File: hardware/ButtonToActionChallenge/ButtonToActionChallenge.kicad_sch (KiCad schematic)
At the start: 4 parts, among them J1 ActionOutput, J2 Button Wires, J3 ActionOutput, J4 ActionTrigger

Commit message: updating button to action challenge PCB to use 12v for button LED
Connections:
- net +12V: now also J2.3 (Pin_3)
- net +5V: no longer J2.3 (Pin_3)

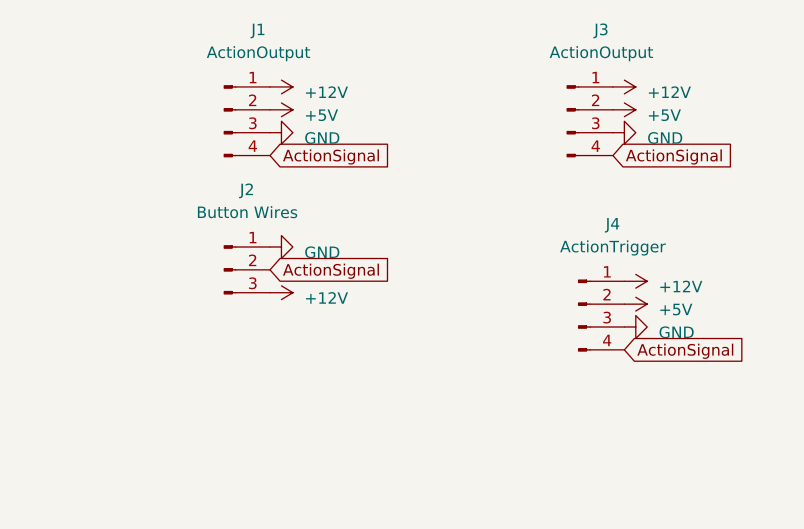
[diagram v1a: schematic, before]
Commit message: Updated Action Challenge Connector Board
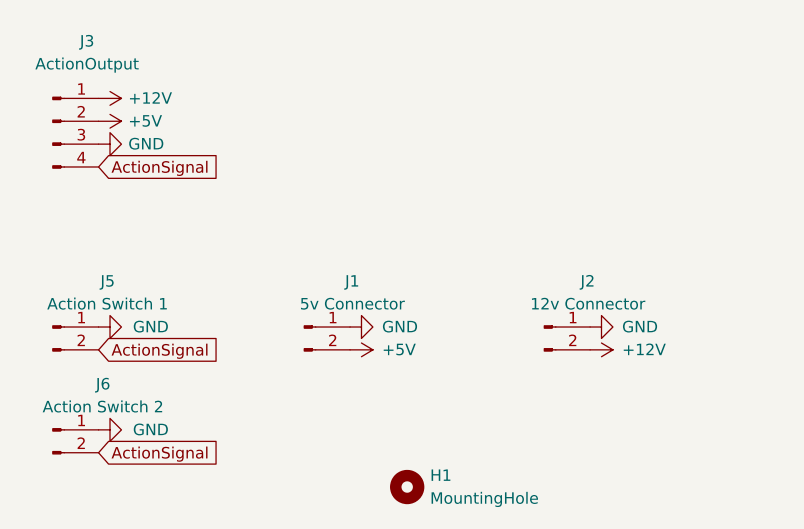
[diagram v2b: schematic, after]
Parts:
- removed J1: ActionOutput, Connector_JST:JST_PH_B4B-PH-K_1x04_P2.00mm_Vertical, symbol Connector:Conn_01x04_Pin
- removed J2: Button Wires, Connector_JST:JST_XH_B3B-XH-A_1x03_P2.50mm_Vertical, symbol Connector:Conn_01x03_Pin
- removed J4: ActionTrigger, Connector_JST:JST_PH_B4B-PH-K_1x04_P2.00mm_Vertical, symbol Connector:Conn_01x04_Pin
- added H1: MountingHole, MountingHole:MountingHole_2.7mm_M2.5, symbol Mechanical:MountingHole
- added J1: 5v Connector, Connector_JST:JST_XH_B2B-XH-A_1x02_P2.50mm_Vertical, symbol Connector:Conn_01x02_Pin
- added J2: 12v Connector, Connector_JST:JST_XH_B2B-XH-A_1x02_P2.50mm_Vertical, symbol Connector:Conn_01x02_Pin
- added J5: Action Switch 1, Connector_JST:JST_XH_B2B-XH-A_1x02_P2.50mm_Vertical, symbol Connector:Conn_01x02_Pin
- added J6: Action Switch 2, Connector_JST:JST_XH_B2B-XH-A_1x02_P2.50mm_Vertical, symbol Connector:Conn_01x02_Pin
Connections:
- net +12V: now also J2.2 (Pin_2)
- net +5V: now also J1.2 (Pin_2)
- net ActionSignal: now also J5.2 (Pin_2), J6.2 (Pin_2)
- net GND: now also J1.1 (Pin_1), J2.1 (Pin_1), J5.1 (Pin_1), J6.1 (Pin_1)
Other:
- moved on the sheet: J3
